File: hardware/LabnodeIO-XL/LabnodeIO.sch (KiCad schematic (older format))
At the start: 6 parts, among them J1 mc 0.5-2.5, J2 EXT3, U1 PCF8574, U2 PCA9685-TSSOP

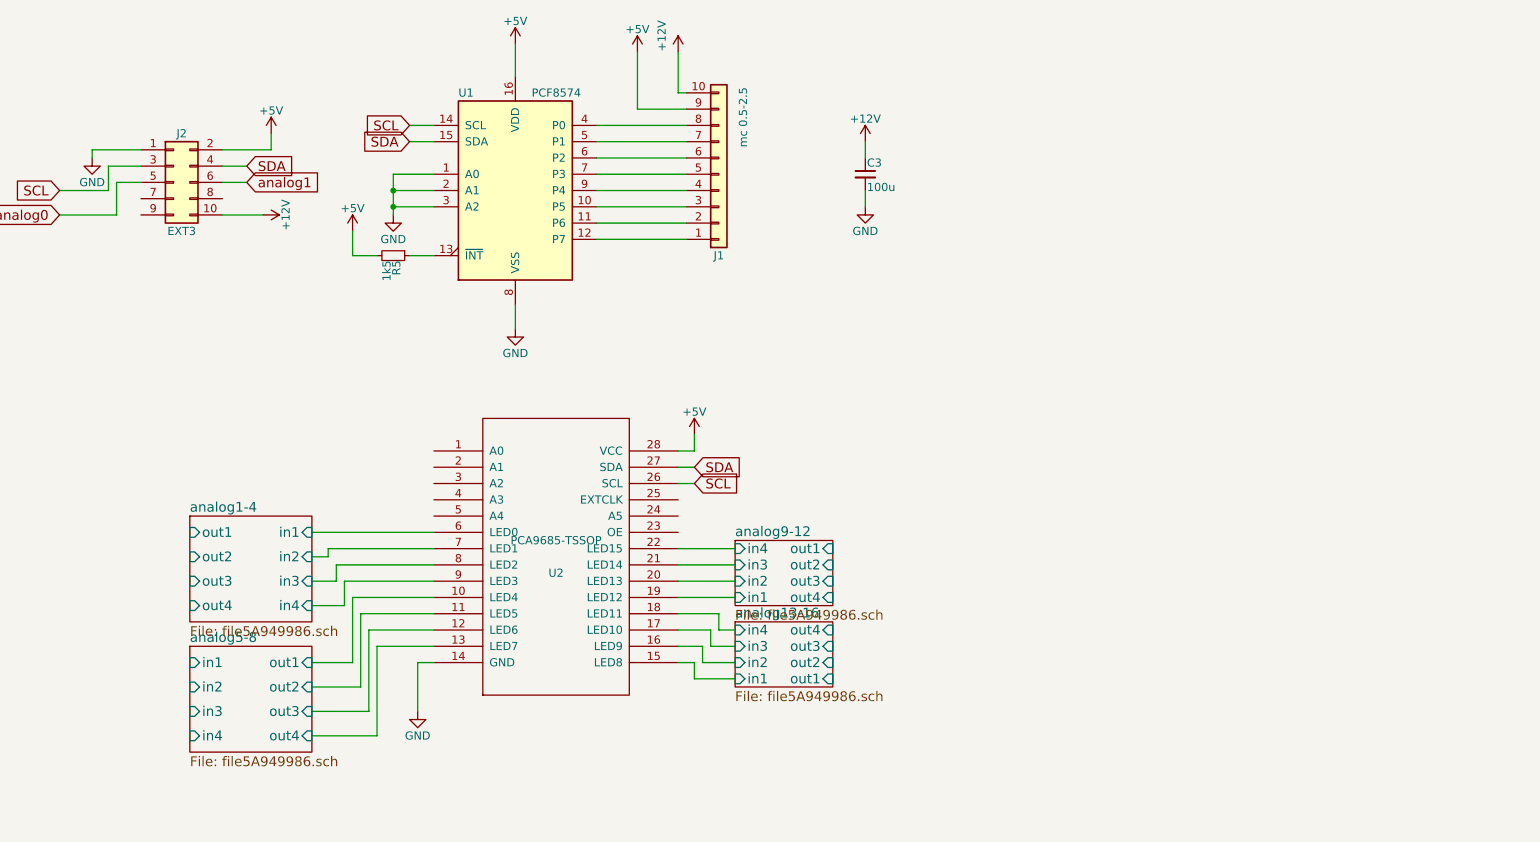
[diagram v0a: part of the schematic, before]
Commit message: Platinenlayout und 3d modell angefangen
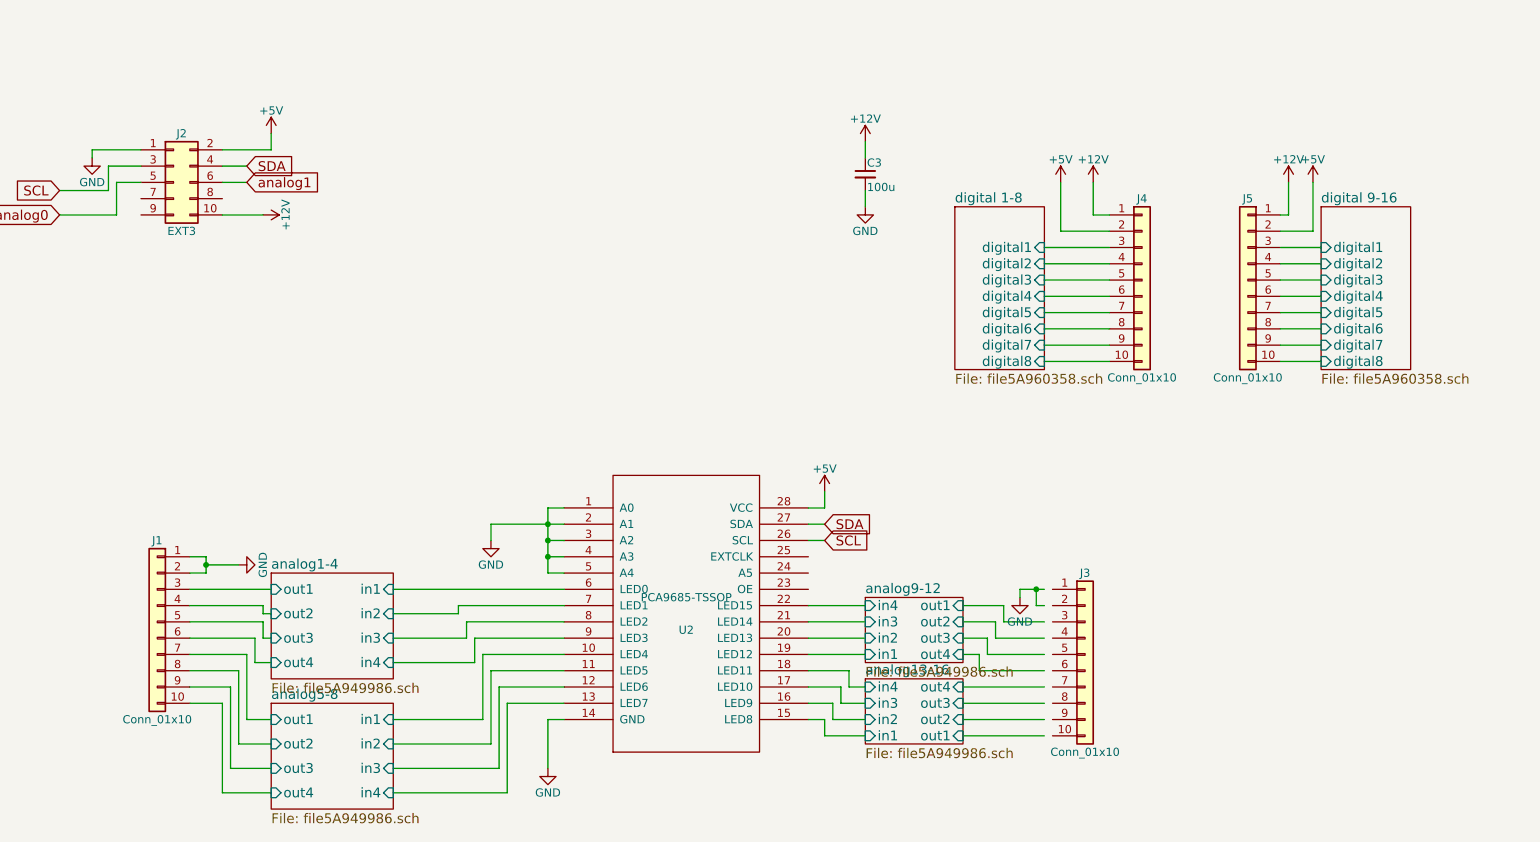
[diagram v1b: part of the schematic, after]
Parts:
- removed R5: 1k5, Resistors_SMD:R_0603_HandSoldering, symbol R_Small
- removed U1: PCF8574, Housings_SOIC:SOIC-16W_7.5x12.8mm_Pitch1.27mm, symbol PCF8574
- added J3, J4, J5: Conn_01x10, mc-0.5-2:MC-0,5-10-G-2,5, symbol Conn_01x10
- J1: value mc 0.5-2.5 -> Conn_01x10; footprint Connectors_Molex:Molex_KK-6410-10_10x2.54mm_Straight -> mc-0.5-2:MC-0,5-10-G-2,5
- U2: footprint MODULE -> Housings_SSOP:TSSOP-28_4.4x9.7mm_Pitch0.65mm
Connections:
- wire segments 82 -> 136
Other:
- moved on the sheet: U2

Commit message: pwm chip geroutet
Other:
- moved on the sheet: J3
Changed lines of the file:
@@
 L Conn_01x10 J3
 U 1 1 5A978AA2
-P 7700 5250
-F 0 "J3" H 7700 5750 50  0000 C CNN
-F 1 "Conn_01x10" H 7700 4650 50  0000 C CNN
-F 2 "mc-0.5-2:MC-0,5-10-G-2,5" H 7700 5250 50  0001 C CNN
-F 3 "" H 7700 5250 50  0001 C CNN
-	1    7700 5250
+P 7650 5250
+F 0 "J3" H 7650 5750 50  0000 C CNN
+F 1 "Conn_01x10" H 7650 4650 50  0000 C CNN
+F 2 "mc-0.5-2:MC-0,5-10-G-2,5" H 7650 5250 50  0001 C CNN
+F 3 "" H 7650 5250 50  0001 C CNN
+	1    7650 5250
 	1    0    0    -1
 $EndComp

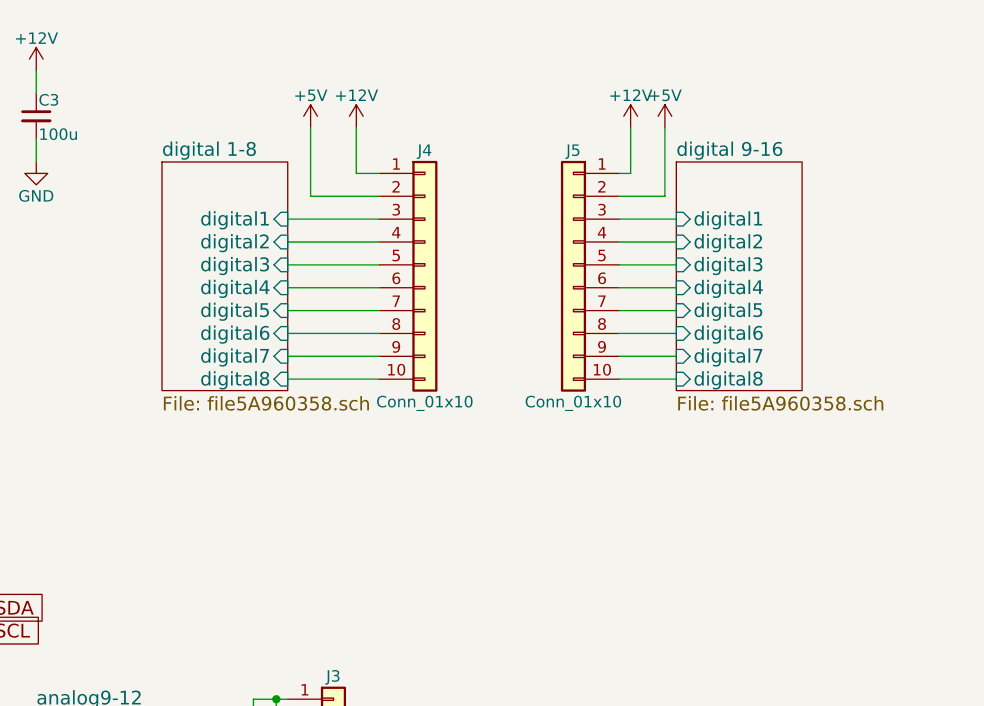
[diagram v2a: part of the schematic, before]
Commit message: eingangswiderstände hinzugefuegt und geroutet
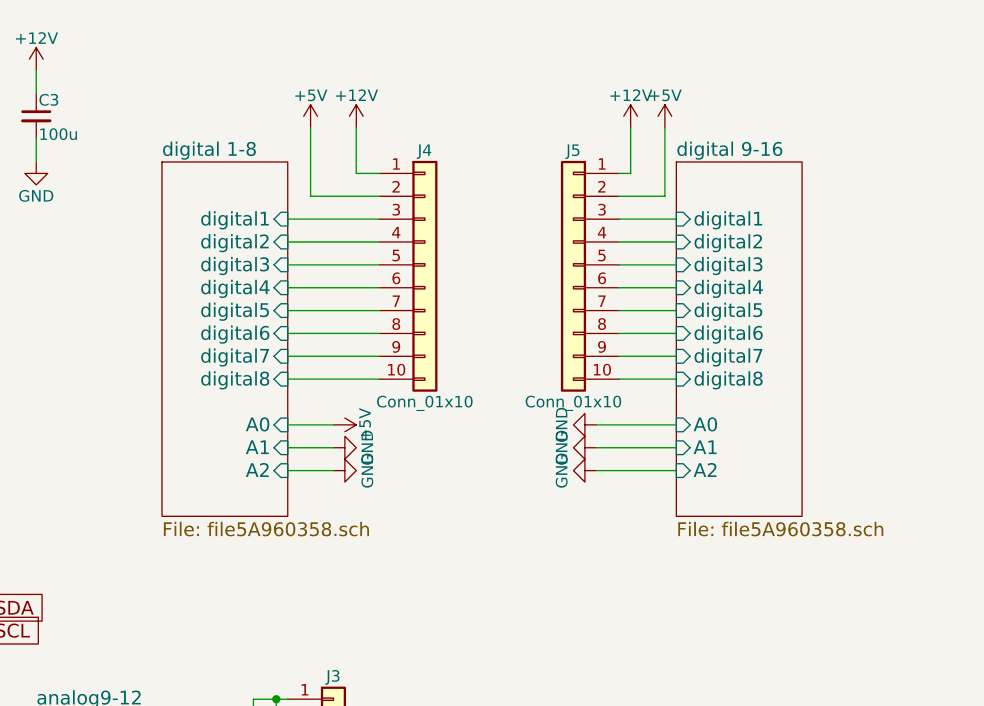
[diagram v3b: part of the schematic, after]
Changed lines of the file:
@@
 $EndComp
 $Comp
-L GND #PWR01
+L GND #PWR1
 U 1 1 5A8D94F9
 P 1600 2200
-F 0 "#PWR01" H 1600 1950 50  0001 C CNN
+F 0 "#PWR1" H 1600 1950 50  0001 C CNN
 F 1 "GND" H 1600 2050 50  0000 C CNN
 F 2 "" H 1600 2200 50  0001 C CNN
@@
 $EndComp
 $Comp
-L +5V #PWR02
+L +5V #PWR4
 U 1 1 5A8D955D
 P 2700 2050
-F 0 "#PWR02" H 2700 1900 50  0001 C CNN
+F 0 "#PWR4" H 2700 1900 50  0001 C CNN
 F 1 "+5V" H 2700 2190 50  0000 C CNN
 F 2 "" H 2700 2050 50  0001 C CNN
@@
 $EndComp
 $Comp
-L +12V #PWR03
+L +12V #PWR8
 U 1 1 5A8DBE7B
 P 6350 2100
-F 0 "#PWR03" H 6350 1950 50  0001 C CNN
+F 0 "#PWR8" H 6350 1950 50  0001 C CNN
 F 1 "+12V" H 6350 2240 50  0000 C CNN
 F 2 "" H 6350 2100 50  0001 C CNN
@@
 $EndComp
 $Comp
-L GND #PWR04
+L GND #PWR9
 U 1 1 5A8DBF15
 P 6350 2500
-F 0 "#PWR04" H 6350 2250 50  0001 C CNN
+F 0 "#PWR9" H 6350 2250 50  0001 C CNN
 F 1 "GND" H 6350 2350 50  0000 C CNN
 F 2 "" H 6350 2500 50  0001 C CNN
@@
 $EndComp
 $Comp
-L +12V #PWR05
+L +12V #PWR3
 U 1 1 5A8EB4AA
 P 2650 2550
-F 0 "#PWR05" H 2650 2400 50  0001 C CNN
+F 0 "#PWR3" H 2650 2400 50  0001 C CNN
 F 1 "+12V" H 2650 2690 50  0000 C CNN
 F 2 "" H 2650 2550 50  0001 C CNN
@@
 $EndComp
 $Comp
-L GND #PWR06
+L GND #PWR6
 U 1 1 5A955CDF
 P 4400 5950
-F 0 "#PWR06" H 4400 5700 50  0001 C CNN
+F 0 "#PWR6" H 4400 5700 50  0001 C CNN
 F 1 "GND" H 4400 5800 50  0000 C CNN
 F 2 "" H 4400 5950 50  0001 C CNN
@@
 	6100 5750 6350 5750
 $Comp
-L +5V #PWR07
+L +5V #PWR7
 U 1 1 5A962F22
 P 6100 4250
-F 0 "#PWR07" H 6100 4100 50  0001 C CNN
+F 0 "#PWR7" H 6100 4100 50  0001 C CNN
 F 1 "+5V" H 6100 4390 50  0000 C CNN
 F 2 "" H 6100 4250 50  0001 C CNN
@@
 	6000 4450 6100 4450
 $Comp
-L GND #PWR08
+L GND #PWR5
 U 1 1 5A95AA82
 P 4050 4550
-F 0 "#PWR08" H 4050 4300 50  0001 C CNN
+F 0 "#PWR5" H 4050 4300 50  0001 C CNN
 F 1 "GND" H 4050 4400 50  0000 C CNN
 F 2 "" H 4050 4550 50  0001 C CNN
@@
 	7200 5050 7450 5050
 $Comp
-L GND #PWR09
+L GND #PWR10
 U 1 1 5A95CBCA
 P 7300 4900
-F 0 "#PWR09" H 7300 4650 50  0001 C CNN
+F 0 "#PWR10" H 7300 4650 50  0001 C CNN
 F 1 "GND" H 7300 4750 50  0000 C CNN
 F 2 "" H 7300 4900 50  0001 C CNN
@@
 	2400 6100 2700 6100
 $Comp
-L GND #PWR010
+L GND #PWR2
 U 1 1 5A95F36C
 P 2500 4700
-F 0 "#PWR010" H 2500 4450 50  0001 C CNN
+F 0 "#PWR2" H 2500 4450 50  0001 C CNN
 F 1 "GND" H 2500 4550 50  0000 C CNN
 F 2 "" H 2500 4700 50  0001 C CNN
@@
 Connection ~ 2300 4700
 $Sheet
-S 6900 2500 550  1000
+S 6900 2500 550  1550
 U 5A960359
 F0 "digital 1-8" 60
@@
 F8 "digital7" I R 7450 3350 60
 F9 "digital8" I R 7450 3450 60
+F10 "A0" I R 7450 3650 60
+F11 "A1" I R 7450 3750 60
+F12 "A2" I R 7450 3850 60
 $EndSheet
 $Comp
-L +5V #PWR011
+L +5V #PWR11
 U 1 1 5A964393
 P 7550 2350
-F 0 "#PWR011" H 7550 2200 50  0001 C CNN
+F 0 "#PWR11" H 7550 2200 50  0001 C CNN
 F 1 "+5V" H 7550 2490 50  0000 C CNN
 F 2 "" H 7550 2350 50  0001 C CNN
@@
 $EndComp
 $Comp
-L +12V #PWR012
+L +12V #PWR15
 U 1 1 5A964854
 P 7750 2350
-F 0 "#PWR012" H 7750 2200 50  0001 C CNN
+F 0 "#PWR15" H 7750 2200 50  0001 C CNN
 F 1 "+12V" H 7750 2490 50  0000 C CNN
 F 2 "" H 7750 2350 50  0001 C CNN
@@
 Wire Wire Line
 	7850 3450 7450 3450
-$Sheet
-S 9150 2500 550  1000
-U 5A960B2A
-F0 "digital 9-16" 60
-F1 "file5A960358.sch" 60
-F2 "digital1" I L 9150 2750 60
-F3 "digital2" I L 9150 2850 60
-F4 "digital3" I L 9150 2950 60
-F5 "digital4" I L 9150 3050 60
-F6 "digital5" I L 9150 3150 60
-F7 "digital6" I L 9150 3250 60
-F8 "digital7" I L 9150 3350 60
-F9 "digital8" I L 9150 3450 60
-$EndSheet
 Wire Wire Line
 	9150 3450 8900 3450
@@
 	8900 2750 9150 2750
 $Comp
-L +12V #PWR013
+L +12V #PWR19
 U 1 1 5A968751
 P 8950 2350
-F 0 "#PWR013" H 8950 2200 50  0001 C CNN
+F 0 "#PWR19" H 8950 2200 50  0001 C CNN
 F 1 "+12V" H 8950 2490 50  0000 C CNN
 F 2 "" H 8950 2350 50  0001 C CNN
@@
 $EndComp
 $Comp
-L +5V #PWR014
+L +5V #PWR20
 U 1 1 5A96889F
 P 9100 2350
-F 0 "#PWR014" H 9100 2200 50  0001 C CNN
+F 0 "#PWR20" H 9100 2200 50  0001 C CNN
 F 1 "+5V" H 9100 2490 50  0000 C CNN
 F 2 "" H 9100 2350 50  0001 C CNN
@@
 F9 "out4" I L 2700 6100 60
 $EndSheet
+$Sheet
+S 9150 2500 550  1550
+U 5A960B2A
+F0 "digital 9-16" 60
+F1 "file5A960358.sch" 60
+F2 "digital1" I L 9150 2750 60
+F3 "digital2" I L 9150 2850 60
+F4 "digital3" I L 9150 2950 60
+F5 "digital4" I L 9150 3050 60
+F6 "digital5" I L 9150 3150 60
+F7 "digital6" I L 9150 3250 60
+F8 "digital7" I L 9150 3350 60
+F9 "digital8" I L 9150 3450 60
+F10 "A0" I L 9150 3650 60
+F11 "A1" I L 9150 3750 60
+F12 "A2" I L 9150 3850 60
+$EndSheet
+$Comp
+L +5V #PWR12
+U 1 1 5A9AA59C
+P 7650 3650
+F 0 "#PWR12" H 7650 3500 50  0001 C CNN
+F 1 "+5V" H 7650 3790 50  0000 C CNN
+F 2 "" H 7650 3650 50  0001 C CNN
+F 3 "" H 7650 3650 50  0001 C CNN
+	1    7650 3650
+	0    1    1    0
+$EndComp
+$Comp
+L GND #PWR13
+U 1 1 5A9AA700
+P 7650 3750
+F 0 "#PWR13" H 7650 3500 50  0001 C CNN
+F 1 "GND" H 7650 3600 50  0000 C CNN
+F 2 "" H 7650 3750 50  0001 C CNN
+F 3 "" H 7650 3750 50  0001 C CNN
+	1    7650 3750
+	0    -1   -1   0
+$EndComp
+$Comp
+L GND #PWR14
+U 1 1 5A9AA9BD
+P 7650 3850
+F 0 "#PWR14" H 7650 3600 50  0001 C CNN
+F 1 "GND" H 7650 3700 50  0000 C CNN
+F 2 "" H 7650 3850 50  0001 C CNN
+F 3 "" H 7650 3850 50  0001 C CNN
+	1    7650 3850
+	0    -1   -1   0
+$EndComp
+$Comp
+L GND #PWR16
+U 1 1 5A9AABCA
+P 8800 3650
+F 0 "#PWR16" H 8800 3400 50  0001 C CNN
+F 1 "GND" H 8800 3500 50  0000 C CNN
+F 2 "" H 8800 3650 50  0001 C CNN
+F 3 "" H 8800 3650 50  0001 C CNN
+	1    8800 3650
+	0    1    1    0
+$EndComp
+$Comp
+L GND #PWR17
+U 1 1 5A9AAD2E
+P 8800 3750
+F 0 "#PWR17" H 8800 3500 50  0001 C CNN
+F 1 "GND" H 8800 3600 50  0000 C CNN
+F 2 "" H 8800 3750 50  0001 C CNN
+F 3 "" H 8800 3750 50  0001 C CNN
+	1    8800 3750
+	0    1    1    0
+$EndComp
+$Comp
+L GND #PWR18
+U 1 1 5A9AAE92
+P 8800 3850
+F 0 "#PWR18" H 8800 3600 50  0001 C CNN
+F 1 "GND" H 8800 3700 50  0000 C CNN
+F 2 "" H 8800 3850 50  0001 C CNN
+F 3 "" H 8800 3850 50  0001 C CNN
+	1    8800 3850
+	0    1    1    0
+$EndComp
+Wire Wire Line
+	8800 3850 9150 3850
+Wire Wire Line
+	9150 3750 8800 3750
+Wire Wire Line
+	8800 3650 9150 3650
+Wire Wire Line
+	7650 3850 7450 3850
+Wire Wire Line
+	7450 3750 7650 3750
+Wire Wire Line
+	7650 3650 7450 3650
 $EndSCHEMATC
